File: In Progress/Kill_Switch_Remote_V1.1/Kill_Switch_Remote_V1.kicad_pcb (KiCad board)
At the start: 4 copper layers, 65 x 27 mm, 60 parts, among them J1 USB_B_Micro, J2 S2B-PH-K-S(LF)(SN), J3 U.FL-R-SMT-1(10), Q2 UMH3N, SW4 AS11CH, U1 ESP32-PICO-MINI-02, U2 CP2102N-A02-GQFN28, U3 LP5912-3.3DRV, U4 MCP73871-2CC-Custom, U5 RFM95W-915S2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

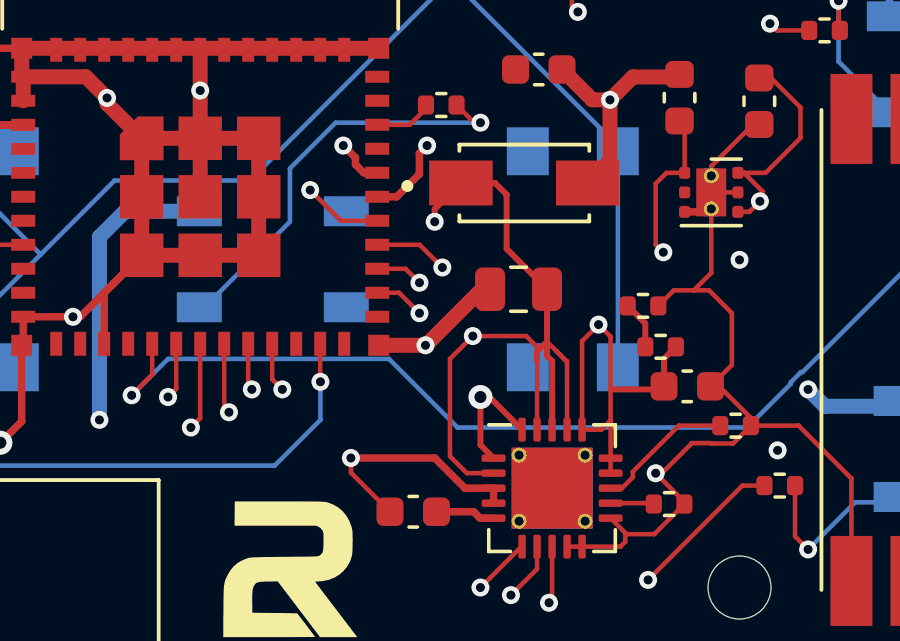
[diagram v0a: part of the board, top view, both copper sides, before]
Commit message: Updates to the kill switches
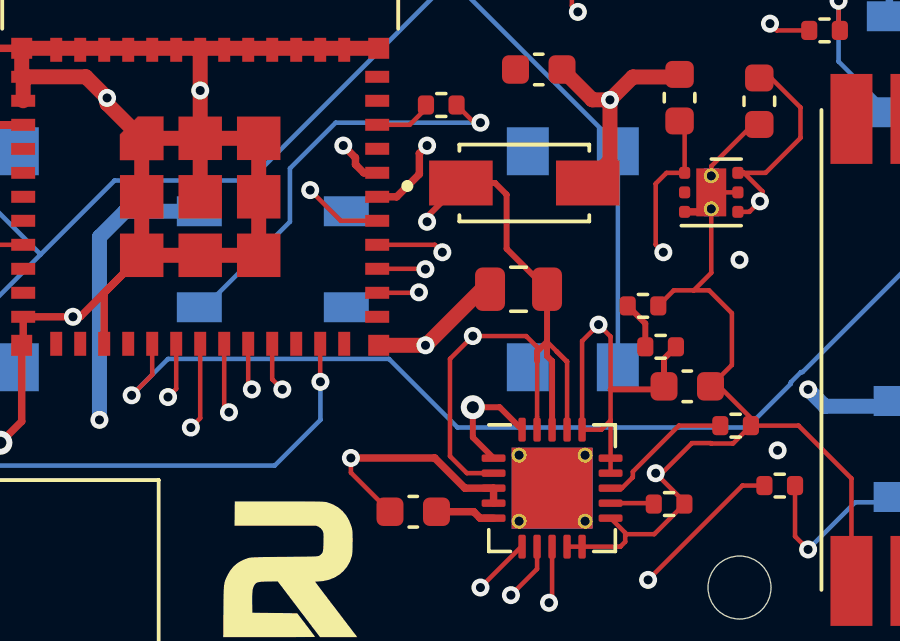
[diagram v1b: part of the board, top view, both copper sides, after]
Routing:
- net +3V3: track 78.8 -> 80.0 mm
- net LORA_LED_DATA: track 21.0 -> 20.2 mm
- net ON_SW_OUT: track 16.6 -> 15.9 mm
- net OFF_SW_OUT: track 15.0 -> 14.4 mm
